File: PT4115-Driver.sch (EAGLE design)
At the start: 21 parts, among them J1 M023.5MM

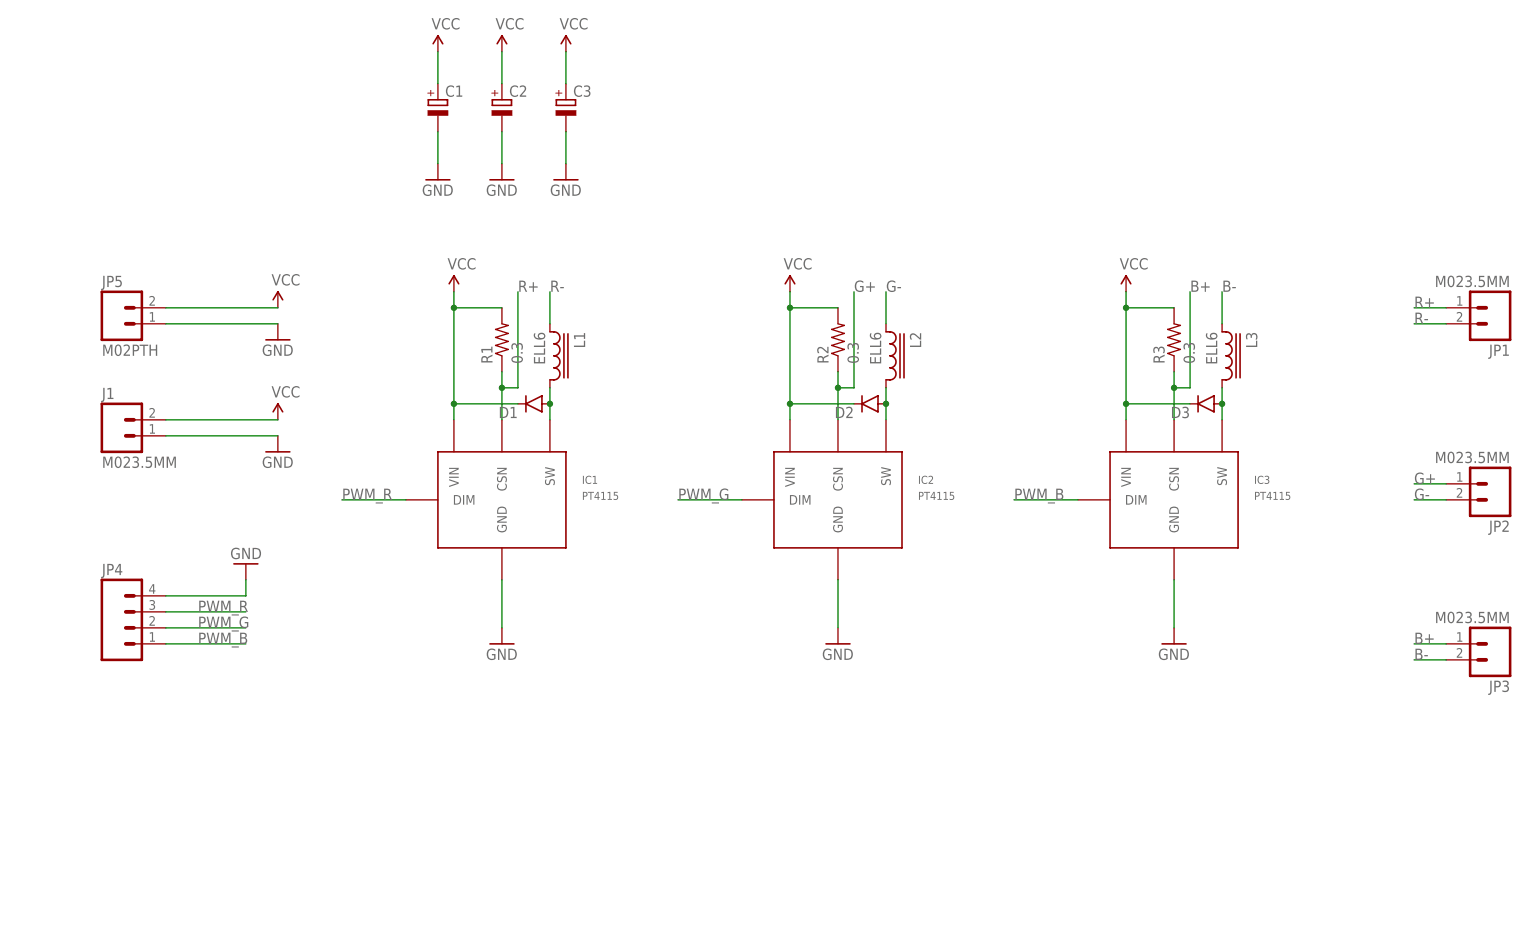
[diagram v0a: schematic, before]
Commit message: Improved schematics and board aesthetics
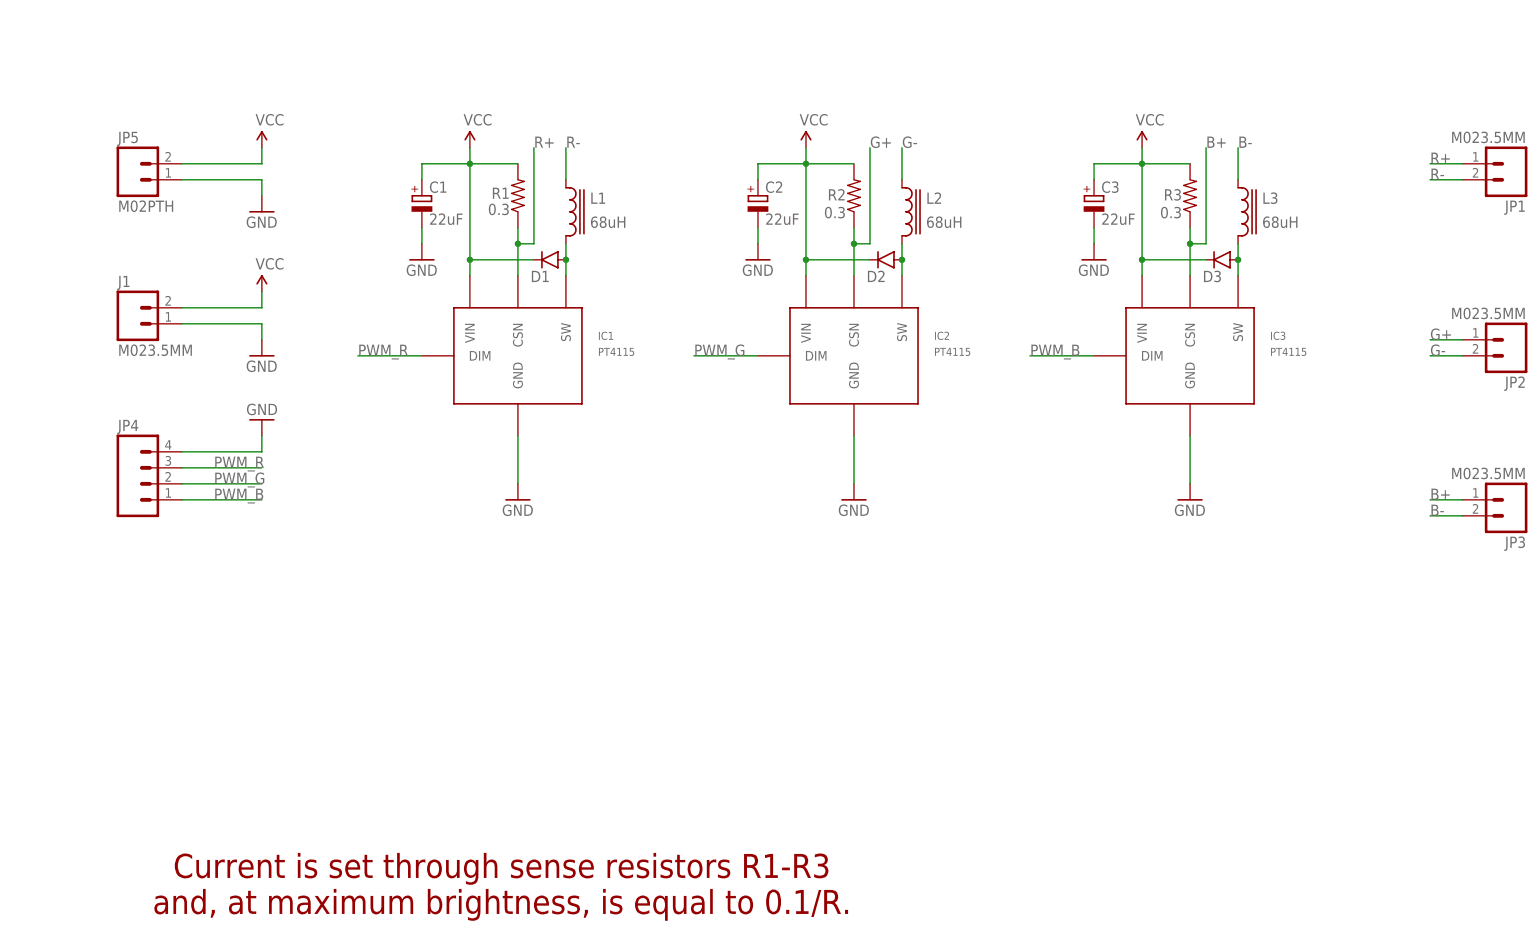
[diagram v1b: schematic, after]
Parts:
- C1, C2, C3: value (none) -> 22uF
- L1, L2, L3: value ELL6 -> 68uH
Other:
- note added: "Current is set through sense resistors R1-R3 and, at maximum brightness, is equal to 0.1/R."
- moved on the sheet: C1, C2, C3, D1, D2, D3, IC1, IC2, IC3, J1, JP1, JP2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
